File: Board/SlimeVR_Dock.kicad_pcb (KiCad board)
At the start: 2 copper layers, 100 x 78 mm, 136 parts, among them J1Fan1 Conn_01x04_Pin, J1Temp1 Conn_01x05_Pin, J1_Control1 Conn_01x03_Pin, J1_MainPW1 USB_C_Receptacle_USB2.0_16P, J1_Monitor1 Conn_01x03_Pin, J1_Prog1 Conn_01x03_Pin, J2 USB_C_Receptacle_USB2.0_16P, J3 USB_C_Receptacle_USB2.0_16P, J4 USB_C_Receptacle_USB2.0_16P, J5 USB_C_Receptacle_USB2.0_16P, J6 USB_C_Receptacle_USB2.0_16P, J7 USB_C_Receptacle_USB2.0_16P, J8 USB_C_Receptacle_USB2.0_16P, J9 USB_C_Receptacle_USB2.0_16P, Q1 NDT452AP, Q2 BC857, Q3 BC857, Q4 BC857, Q5 BC857, Q6 BC817, U1 ESP32-C3-WROOM-02, U10 INA226, U11 AP22652W6-7, U12 INA226, U13 INA226, U14 AP22652W6-7, U15 INA226, U16 INA226, U17 74HC165, U18 74HC165, U19 74HC595, U2 CH224K, U3 XC6220B331MR, U4 TPS548A20RVER, U5 AP22652W6-7, U6 INA226, U7 INA226, U8 AP22652W6-7, U9 INA226

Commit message: Changed baed on sugestions
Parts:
- removed D2: 5.1V, Diode_SMD:D_SOD-123
- added R56: 100k, Resistor_SMD:R_0603_1608Metric, B.Cu at (110.0, 122.7)
- added R57: 10k, Resistor_SMD:R_0603_1608Metric, F.Cu at (113.9, 123.4)
- R37: value 4k7 -> 75k
- moved C27 0.32 mm to (115.0, 119.4), turned to 90 degrees
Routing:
- net Net-(C27-Pad1): track 3.26 -> 2.46 mm
- net Net-(U4-PGOOD): track 5.15 -> 5.94 mm

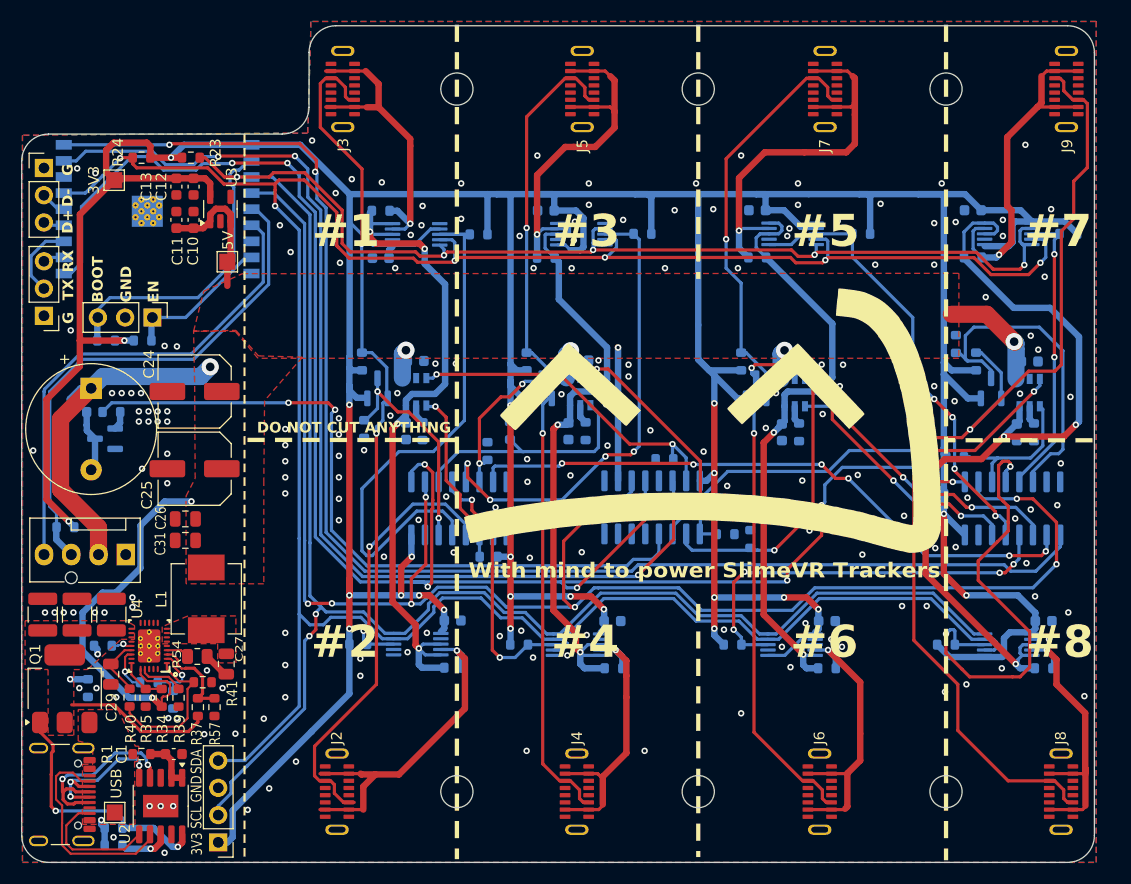
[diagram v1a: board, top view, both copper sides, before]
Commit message: added caps to outputs
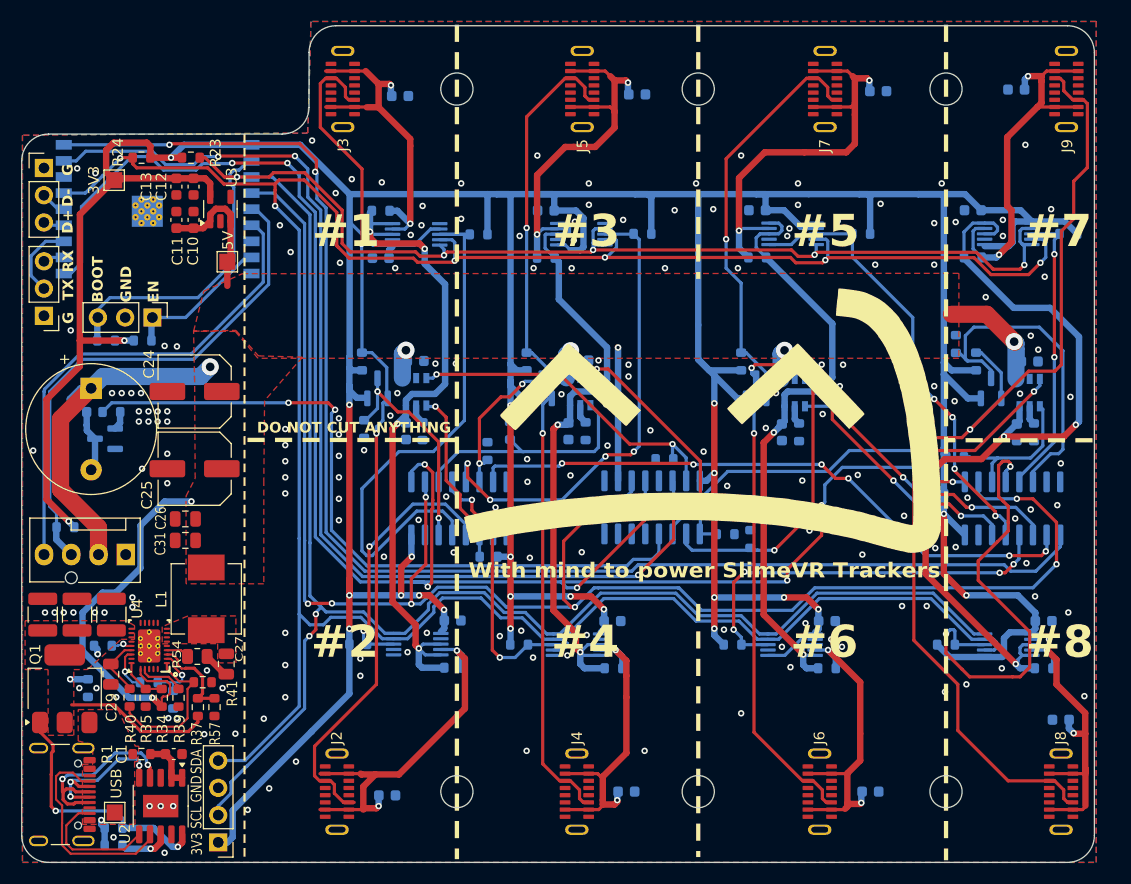
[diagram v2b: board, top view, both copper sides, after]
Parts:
- added C28: 100nF, Capacitor_SMD:C_0603_1608Metric, B.Cu at (130.0, 131.7)
- added C32: 100nF, Capacitor_SMD:C_0603_1608Metric, B.Cu at (131.2, 66.5)
- added C33: 100nF, Capacitor_SMD:C_0603_1608Metric, B.Cu at (153.3, 66.3)
- added C34: 100nF, Capacitor_SMD:C_0603_1608Metric, B.Cu at (152.3, 131.3)
- added C35: 100nF, Capacitor_SMD:C_0603_1608Metric, B.Cu at (175.8, 66.0)
- added C36: 100nF, Capacitor_SMD:C_0603_1608Metric, B.Cu at (175.1, 131.3)
- added C37: 100nF, Capacitor_SMD:C_0603_1608Metric, B.Cu at (188.7, 65.8)
- added C38: 100nF, Capacitor_SMD:C_0603_1608Metric, B.Cu at (192.8, 124.6)
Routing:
- net Net-(U16-Vin-): track 31.7 -> 34.4 mm, vias 1 -> 2
- net Net-(U15-Vin-): track 26.7 -> 29.3 mm, vias 1 -> 2
- net Net-(U6-Vin-): track 32.9 -> 35.4 mm, vias 1 -> 2
- net Net-(U10-Vin-): track 32.1 -> 34.5 mm, vias 1 -> 2
- net Net-(U13-Vin-): track 37.1 -> 39.5 mm, vias 1 -> 2
- net Net-(U9-Vin-): track 26.5 -> 28.9 mm, vias 1 -> 2
- net Net-(U12-Vin-): track 27.0 -> 29.4 mm, vias 1 -> 2
- net Net-(U7-Vin-): track 28.9 -> 31.1 mm, vias 1 -> 2

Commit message: updated by sugestions
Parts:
- added C39: 100nF, Capacitor_SMD:C_0805_2012Metric, F.Cu at (111.2, 103.9)
- moved C25 1.70 mm to (112.2, 99.5)
- moved C24 1.66 mm to (112.1, 92.3)
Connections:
- R56 pad 1: Earth -> Net-(U4-VREG)
- U4 pad V: Earth -> (no net)
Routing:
- net Net-(U4-VREG): track 5.63 -> 14.5 mm, vias 0 -> 1
- net Earth: vias 183 -> 185

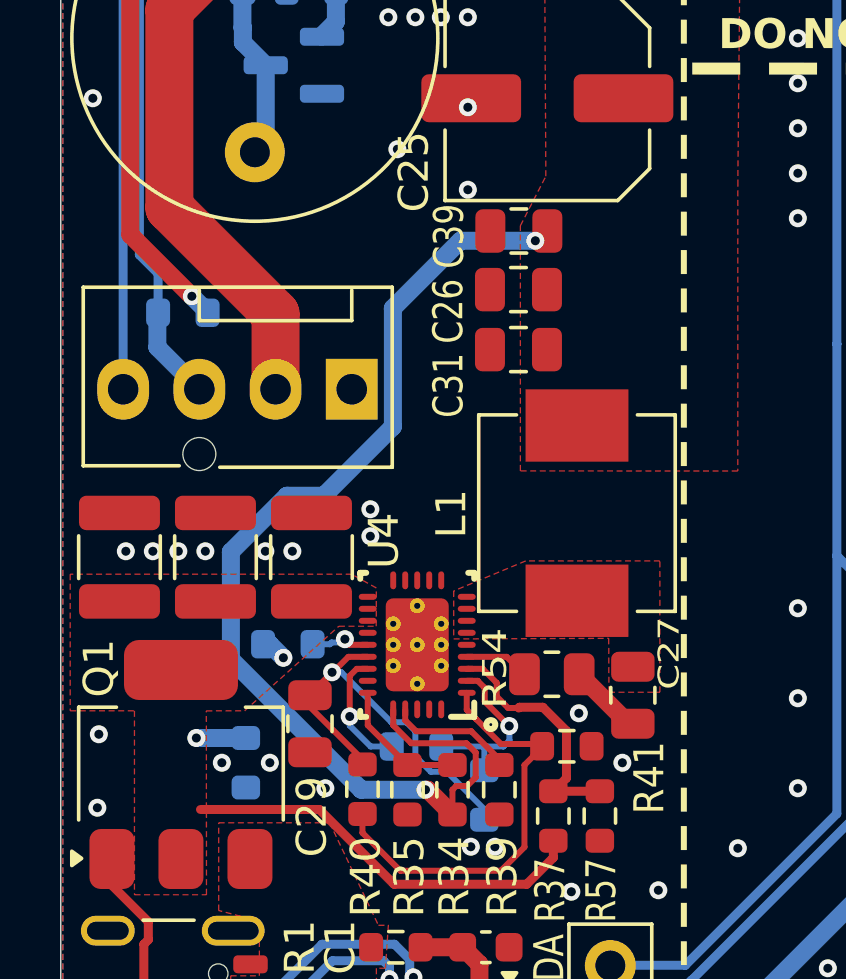
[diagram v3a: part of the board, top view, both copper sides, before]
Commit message: fixed via in pad
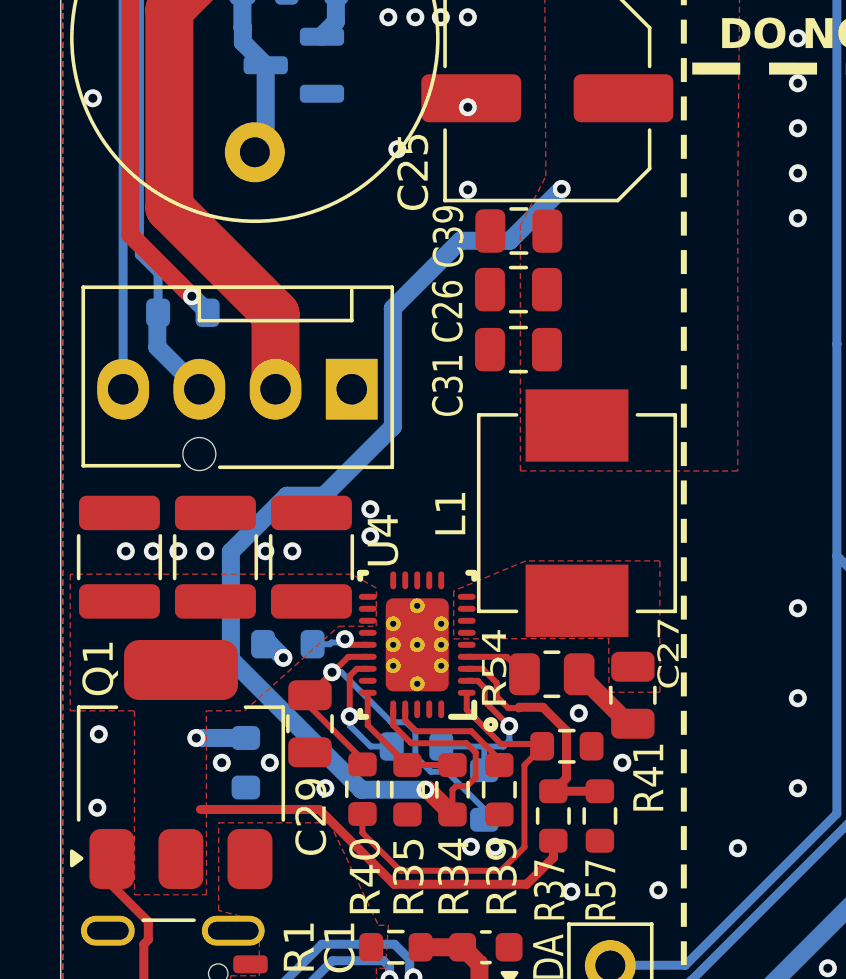
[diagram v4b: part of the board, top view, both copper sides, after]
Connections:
- U4 pad V: (no net) -> Earth
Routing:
- net 5VStepDown: track 128.3 -> 129.9 mm
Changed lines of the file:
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@@
 			(layers "*.Cu" "*.Mask")
 			(remove_unused_layers no)
+			(net "Earth")
 		)
 		(pad "V" thru_hole circle
@@
 			(layers "*.Cu" "*.Mask")
 			(remove_unused_layers no)
+			(net "Earth")
 		)
 		(pad "V" thru_hole circle
@@
 			(layers "*.Cu" "*.Mask")
 			(remove_unused_layers no)
+			(net "Earth")
 		)
 		(pad "V" thru_hole circle
@@
 			(layers "*.Cu" "*.Mask")
 			(remove_unused_layers no)
+			(net "Earth")
 		)
 		(embedded_fonts no)
@@
 	)
 	(via
-		(at 111.75 104.25)
+		(at 112.625 102.525)
 		(size 0.6)
 		(drill 0.3)
@@
 	)
 	(segment
-		(start 107 110.45)
-		(end 107 106.5)
+		(start 104.7 112.75)
+		(end 103.468629 112.75)
 		(width 0.6)
 		(layer "B.Cu")
@@
 	)
 	(segment
-		(start 107 106.5)
-		(end 109.25 104.25)
+		(start 101.6 114.618629)
+		(end 101.6 118.2)
 		(width 0.6)
 		(layer "B.Cu")
@@
 	)
 	(segment
-		(start 109.25 104.25)
-		(end 111.75 104.25)
-		(width 0.6)
-		(layer "B.Cu")
-		(net "5VStepDown")
-	)
-	(segment
 		(start 131.749998 90.150002)
 		(end 131.75 90.15)
@@
 	)
 	(segment
-		(start 101.6 114.618629)
-		(end 103.468629 112.75)
+		(start 100.4125 95.9125)
+		(end 100.4125 94.6875)
 		(width 0.6)
 		(layer "B.Cu")
@@
 	)
 	(segment
-		(start 100.4125 95.9125)
-		(end 100.4125 94.6875)
+		(start 112.625 102.525)
+		(end 110.9 104.25)
+		(width 0.6)
+		(layer "B.Cu")
+		(net "5VStepDown")
+	)
+	(segment
+		(start 101.6 118.2)
+		(end 105.95 122.55)
 		(width 0.6)
 		(layer "B.Cu")
@@
 	)
 	(segment
+		(start 107 110.45)
+		(end 104.7 112.75)
+		(width 0.6)
+		(layer "B.Cu")
+		(net "5VStepDown")
+	)
+	(segment
 		(start 147.049999 91.275001)
 		(end 147.225 91.1)
@@
 	)
 	(segment
-		(start 104.7 112.75)
-		(end 107 110.45)
+		(start 103.468629 112.75)
+		(end 101.6 114.618629)
 		(width 0.6)
 		(layer "B.Cu")
@@
 	)
 	(segment
+		(start 105.95 122.55)
+		(end 108.0875 122.55)
+		(width 0.6)
+		(layer "B.Cu")
+		(net "5VStepDown")
+	)
+	(segment
 		(start 131.4196 90.4804)
 		(end 131.4196 92.75)
@@
 	)
 	(segment
-		(start 101.6 118.2)
-		(end 101.6 114.618629)
+		(start 109.25 104.25)
+		(end 107 106.5)
 		(width 0.6)
 		(layer "B.Cu")
@@
 	)
 	(segment
+		(start 107 106.5)
+		(end 107 110.45)
+		(width 0.6)
+		(layer "B.Cu")
+		(net "5VStepDown")
+	)
+	(segment
 		(start 103.5 92.6)
 		(end 102.4 93.7)
@@
 	)
 	(segment
-		(start 103.468629 112.75)
-		(end 104.7 112.75)
-		(width 0.6)
-		(layer "B.Cu")
-		(net "5VStepDown")
-	)
-	(segment
 		(start 189.125 91.2)
 		(end 189.125 90.025)
@@
 	)
 	(segment
-		(start 108.0875 122.55)
-		(end 105.95 122.55)
-		(width 0.6)
-		(layer "B.Cu")
-		(net "5VStepDown")
-	)
-	(segment
 		(start 151.525 89.9)
 		(end 151.525 102.325)
@@
 	)
 	(segment
-		(start 105.95 122.55)
-		(end 101.6 118.2)
+		(start 110.9 104.25)
+		(end 109.25 104.25)
 		(width 0.6)
 		(layer "B.Cu")

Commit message: caps reorangement
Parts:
- moved C31 4.88 mm to (108.7, 112.1), turned to -90 degrees
- moved C39 3.94 mm to (111.5, 107.9)
- moved C24 3.80 mm to (112.2, 96.2)
- moved C25 3.80 mm to (112.2, 103.3)
- moved C26 3.73 mm to (108.7, 108.7), turned to 90 degrees
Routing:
- net 5VStepDown: track 129.9 -> 128.4 mm
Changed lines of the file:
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@@
 	(footprint "Capacitor_SMD:C_Elec_6.3x5.4"
 		(layer "F.Cu")
-		(at 112.144048 92.345536 180)
+		(at 112.15 96.15 180)
 		(descr "SMD capacitor, aluminum electrolytic nonpolar, 6.3x5.4mm")
 		(tags "capacitor electrolytic nonpolar")
@@
 	(footprint "Capacitor_SMD:C_0805_2012Metric"
 		(layer "F.Cu")
-		(at 111.1875 105.879 180)
+		(at 108.7 108.660717 90)
 		(descr "Capacitor SMD 0805 (2012 Metric), square (rectangular) end terminal, IPC-7351 nominal, (Body size source: IPC-SM-782 page 76, https://www.pcb-3d.com/wordpress/wp-content/uploads/ipc-sm-782a_amendment_1_and_2.pdf, https://docs.google.com/spreadsheets/d/1BsfQQcO9C6DZCsRaXUlFlo91Tg2WpOkGARC1WS5S8t0/edit?usp=sharing), generated with kicad-footprint-generator")
 		(tags "capacitor")
 		(property "Reference" "C26"
-			(at 2.3375 -0.721 90)
+			(at 0.010717 -1.2 90)
 			(layer "F.SilkS")
 			(effects
 				(font
-					(size 1 0.8)
+					(size 0.8 0.8)
 					(thickness 0.15)
 				)
@@
 		)
 		(property "Value" "47uF"
-			(at 0 1.68 0)
+			(at 0 1.68 90)
 			(layer "F.Fab")
 			(effects
@@
 		)
 		(property "Datasheet" ""
-			(at 0 0 0)
+			(at 0 0 90)
 			(layer "F.Fab")
 			(hide yes)
@@
 		)
 		(property "Description" "Unpolarized capacitor"
-			(at 0 0 0)
+			(at 0 0 90)
 			(layer "F.Fab")
 			(hide yes)
@@
 		(duplicate_pad_numbers_are_jumpers no)
 		(fp_line
-			(start -0.261252 0.735)
-			(end 0.261252 0.735)
+			(start -0.261252 -0.735)
+			(end 0.261252 -0.735)
 			(stroke
 				(width 0.12)
@@
 		)
 		(fp_line
-			(start -0.261252 -0.735)
-			(end 0.261252 -0.735)
+			(start -0.261252 0.735)
+			(end 0.261252 0.735)
 			(stroke
 				(width 0.12)
@@
 		)
 		(fp_text user "${REFERENCE}"
-			(at 0 0 0)
+			(at 0 0 90)
 			(layer "F.Fab")
 			(effects
@@
 		)
 		(pad "1" smd roundrect
-			(at -0.95 0 180)
+			(at -0.95 0 90)
 			(size 1 1.45)
 			(layers "F.Cu" "F.Mask" "F.Paste")
@@
 		)
 		(pad "2" smd roundrect
-			(at 0.95 0 180)
+			(at 0.95 0 90)
 			(size 1 1.45)
 			(layers "F.Cu" "F.Mask" "F.Paste")
@@
 	(footprint "Capacitor_SMD:C_0805_2012Metric"
 		(layer "F.Cu")
-		(at 111.1875 107.879 180)
+		(at 108.7 112.075 -90)
 		(descr "Capacitor SMD 0805 (2012 Metric), square (rectangular) end terminal, IPC-7351 nominal, (Body size source: IPC-SM-782 page 76, https://www.pcb-3d.com/wordpress/wp-content/uploads/ipc-sm-782a_amendment_1_and_2.pdf, https://docs.google.com/spreadsheets/d/1BsfQQcO9C6DZCsRaXUlFlo91Tg2WpOkGARC1WS5S8t0/edit?usp=sharing), generated with kicad-footprint-generator")
 		(tags "capacitor")
 		(property "Reference" "C31"
-			(at 2.331842 -1.192804 90)
+			(at 0 1.175 90)
 			(layer "F.SilkS")
 			(effects
 				(font
-					(size 1 0.8)
+					(size 0.8 0.8)
 					(thickness 0.15)
 				)
@@
 		)
 		(property "Value" "47uF"
-			(at 0 1.68 0)
+			(at 0 1.68 90)
 			(layer "F.Fab")
 			(effects
@@
 		)
 		(property "Datasheet" ""
-			(at 0 0 0)
+			(at 0 0 90)
 			(layer "F.Fab")
 			(hide yes)
@@
 		)
 		(property "Description" "Unpolarized capacitor"
-			(at 0 0 0)
+			(at 0 0 90)
 			(layer "F.Fab")
 			(hide yes)
@@
 		)
 		(fp_text user "${REFERENCE}"
-			(at 0 0 0)
+			(at 0 0 90)
 			(layer "F.Fab")
 			(effects
@@
 		)
 		(pad "1" smd roundrect
-			(at -0.95 0 180)
+			(at -0.95 0 270)
 			(size 1 1.45)
 			(layers "F.Cu" "F.Mask" "F.Paste")
@@
 		)
 		(pad "2" smd roundrect
-			(at 0.95 0 180)
+			(at 0.95 0 270)
 			(size 1 1.45)
 			(layers "F.Cu" "F.Mask" "F.Paste")
@@
 	(footprint "Capacitor_SMD:C_Elec_6.3x5.4"
 		(layer "F.Cu")
-		(at 112.15 99.5 180)
+		(at 112.15 103.3 180)
 		(descr "SMD capacitor, aluminum electrolytic nonpolar, 6.3x5.4mm")
 		(tags "capacitor electrolytic nonpolar")
 		(property "Reference" "C25"
-			(at 4.45 -2.452 90)
+			(at -4.150503 2.390925 90)
 			(layer "F.SilkS")
 			(effects
@@
 		(tags "inductor vishay ihlp smd")
 		(property "Reference" "L1"
-			(at -0.021 -4.1875 90)
+			(at -1.021 -4.1125 90)
 			(layer "F.SilkS")
 			(effects
@@
 	(footprint "Capacitor_SMD:C_0805_2012Metric"
 		(layer "F.Cu")
-		(at 111.2 103.925)
+		(at 111.462601 107.852176)
 		(descr "Capacitor SMD 0805 (2012 Metric), square (rectangular) end terminal, IPC-7351 nominal, (Body size source: IPC-SM-782 page 76, https://www.pcb-3d.com/wordpress/wp-content/uploads/ipc-sm-782a_amendment_1_and_2.pdf, https://docs.google.com/spreadsheets/d/1BsfQQcO9C6DZCsRaXUlFlo91Tg2WpOkGARC1WS5S8t0/edit?usp=sharing)")
 		(tags "capacitor")
 		(property "Reference" "C39"
-			(at -2.325 0.175 90)
+			(at 2.486848 -0.063741 90)
 			(layer "F.SilkS")
 			(effects
@@
 	)
 	(via
-		(at 108.6 95.85)
+		(at 109 97.425)
 		(size 0.6)
 		(drill 0.3)
@@
 	)
 	(via
-		(at 109.5 95.85)
+		(at 109.9 97.425)
 		(size 0.6)
 		(drill 0.3)
@@
 	)
 	(via
-		(at 107.75 95.85)
+		(at 108.15 97.425)
 		(size 0.6)
 		(drill 0.3)
@@
 	)
 	(via
-		(at 107.15 101.2)
+		(at 107.15 103.275)
 		(size 0.6)
 		(drill 0.3)
@@
 	)
 	(via
-		(at 107.75 96.8)
+		(at 108.15 98.375)
 		(size 0.6)
 		(drill 0.3)
@@
 	)
 	(via
-		(at 109.5 102.55)
+		(at 109.725 105.525)
 		(size 0.6)
 		(drill 0.3)
@@
 	)
 	(via
-		(at 108.6 96.8)
+		(at 109 98.375)
 		(size 0.6)
 		(drill 0.3)
@@
 	)
 	(via
-		(at 109.5 99.8)
+		(at 109.875 102)
 		(size 0.6)
 		(drill 0.3)
@@
 	)
 	(via
-		(at 106.85 95.85)
+		(at 107.25 97.425)
 		(size 0.6)
 		(drill 0.3)
@@
 	)
 	(via
-		(at 109.5 96.8)
+		(at 109.9 98.375)
 		(size 0.6)
 		(drill 0.3)
@@
 	)
 	(via
-		(at 106.85 96.8)
+		(at 107.25 98.375)
 		(size 0.6)
 		(drill 0.3)
@@
 	)
 	(via
-		(at 112.625 102.525)
+		(at 112.05 104.7)
 		(size 0.6)
 		(drill 0.3)
@@
 	)
 	(segment
-		(start 104.7 112.75)
-		(end 103.468629 112.75)
-		(width 0.6)
-		(layer "B.Cu")
-		(net "5VStepDown")
-	)
-	(segment
 		(start 146.7196 90.5804)
 		(end 146.7196 92.72365)
@@
 	)
 	(segment
-		(start 101.6 114.618629)
-		(end 101.6 118.2)
-		(width 0.6)
-		(layer "B.Cu")
-		(net "5VStepDown")
-	)
-	(segment
 		(start 189.125 90.025)
 		(end 188.5 89.4)
@@
 	)
 	(segment
-		(start 112.625 102.525)
-		(end 110.9 104.25)
-		(width 0.6)
-		(layer "B.Cu")
-		(net "5VStepDown")
-	)
-	(segment
-		(start 101.6 118.2)
-		(end 105.95 122.55)
+		(start 107 106.5)
+		(end 107 110.45)
 		(width 0.6)
 		(layer "B.Cu")
@@
 	)
 	(segment
-		(start 107 110.45)
-		(end 104.7 112.75)
-		(width 0.6)
-		(layer "B.Cu")
-		(net "5VStepDown")
-	)
-	(segment
 		(start 147.049999 91.275001)
 		(end 147.225 91.1)
@@
 	)
 	(segment
-		(start 103.468629 112.75)
-		(end 101.6 114.618629)
-		(width 0.6)
-		(layer "B.Cu")
-		(net "5VStepDown")
-	)
-	(segment
 		(start 167.049999 90.169607)
 		(end 167.049272 90.16888)
@@
 	)
 	(segment
+		(start 103.468629 112.75)
+		(end 101.6 114.618629)
+		(width 0.6)
+		(layer "B.Cu")
+		(net "5VStepDown")
+	)
+	(segment
 		(start 147.049999 91.7)
 		(end 147.049999 90.250001)
@@
 	)
 	(segment
-		(start 105.95 122.55)
-		(end 108.0875 122.55)
+		(start 112.05 104.7)
+		(end 108.8 104.7)
 		(width 0.6)
 		(layer "B.Cu")
@@
 	)
 	(segment
-		(start 109.25 104.25)
+		(start 101.6 114.618629)
+		(end 101.6 118.2)
+		(width 0.6)
+		(layer "B.Cu")
+		(net "5VStepDown")
+	)
+	(segment
+		(start 108.8 104.7)
 		(end 107 106.5)
 		(width 0.6)
@@
 	)
 	(segment
-		(start 107 106.5)
-		(end 107 110.45)
+		(start 104.7 112.75)
+		(end 103.468629 112.75)
 		(width 0.6)
 		(layer "B.Cu")
@@
 	)
 	(segment
+		(start 105.95 122.55)
+		(end 108.0875 122.55)
+		(width 0.6)
+		(layer "B.Cu")
+		(net "5VStepDown")
+	)
+	(segment
 		(start 131.749998 91.9)
 		(end 131.749998 90.150002)
@@
 	)
 	(segment
-		(start 110.9 104.25)
-		(end 109.25 104.25)
+		(start 107 110.45)
+		(end 104.7 112.75)
 		(width 0.6)
 		(layer "B.Cu")
@@
 	)
 	(segment
+		(start 101.6 118.2)
+		(end 105.95 122.55)
+		(width 0.6)
+		(layer "B.Cu")
+		(net "5VStepDown")
+	)
+	(segment
 		(start 128.9 129.7)
 		(end 127.6 129.7)
@@
 		(polygon
 			(pts
-				(xy 118.569831 94.850187) (xy 118.5 102.248) (xy 118.497353 111.924983) (xy 111.25 111.923) (xy 111.25 103.75)
-				(xy 112.1 102.099849) (xy 112.05 93.1) (xy 112.046113 93.097309) (xy 111.953392 88.377532) (xy 115.9 88.3)
-				(xy 117.996112 90.67782) (xy 122.1 90.8)
+				(xy 118.569831 94.850187) (xy 118.5 102.248) (xy 118.497353 111.924983) (xy 107.794322 111.903874)
+				(xy 107.779573 108.891256) (xy 111.1 108.875) (xy 111.1 105.3) (xy 112.1 102.099849) (xy 112.05 93.1)
+				(xy 112.046113 93.097309) (xy 111.953392 88.377532) (xy 115.9 88.3) (xy 117.996112 90.67782) (xy 122.1 90.8)
 			)
 		)
